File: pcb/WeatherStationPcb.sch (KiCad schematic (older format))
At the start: 7 parts, among them J1 Screw_Terminal_01x02, J2 Conn_01x06, J3 Conn_01x04, U1 MCP1755S-3302xCB, U3 ESP-01

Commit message: feat(pcb): update pcb
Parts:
- C1: value 100nF -> 10nF
- C2: value 10uF -> 10nF
- J2: value Conn_01x06 -> BME280
- J3: value Conn_01x04 -> BMP280
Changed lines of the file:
@@
 P 5400 2800
 F 0 "J3" V 5272 2980 50  0000 L CNN
-F 1 "Conn_01x04" V 5363 2980 50  0000 L CNN
+F 1 "BMP280" V 5363 2980 50  0000 L CNN
 F 2 "Connector_PinSocket_2.54mm:PinSocket_1x04_P2.54mm_Vertical" H 5400 2800 50  0001 C CNN
 F 3 "~" H 5400 2800 50  0001 C CNN
@@
 P 4150 2800
 F 0 "J2" V 4022 3080 50  0000 L CNN
-F 1 "Conn_01x06" V 4113 3080 50  0000 L CNN
+F 1 "BME280" V 4113 3080 50  0000 L CNN
 F 2 "Connector_PinSocket_2.54mm:PinSocket_1x06_P2.54mm_Vertical" H 4150 2800 50  0001 C CNN
 F 3 "~" H 4150 2800 50  0001 C CNN
@@
 P 3250 2550
 F 0 "C2" H 3365 2596 50  0000 L CNN
-F 1 "10uF" H 3365 2505 50  0000 L CNN
+F 1 "10nF" H 3365 2505 50  0000 L CNN
 F 2 "Capacitor_SMD:C_0805_2012Metric_Pad1.15x1.40mm_HandSolder" H 3288 2400 50  0001 C CNN
 F 3 "~" H 3250 2550 50  0001 C CNN
@@
 P 2100 2550
 F 0 "C1" H 2215 2596 50  0000 L CNN
-F 1 "100nF" H 2215 2505 50  0000 L CNN
+F 1 "10nF" H 2215 2505 50  0000 L CNN
 F 2 "Capacitor_SMD:C_0805_2012Metric_Pad1.15x1.40mm_HandSolder" H 2138 2400 50  0001 C CNN
 F 3 "~" H 2100 2550 50  0001 C CNN

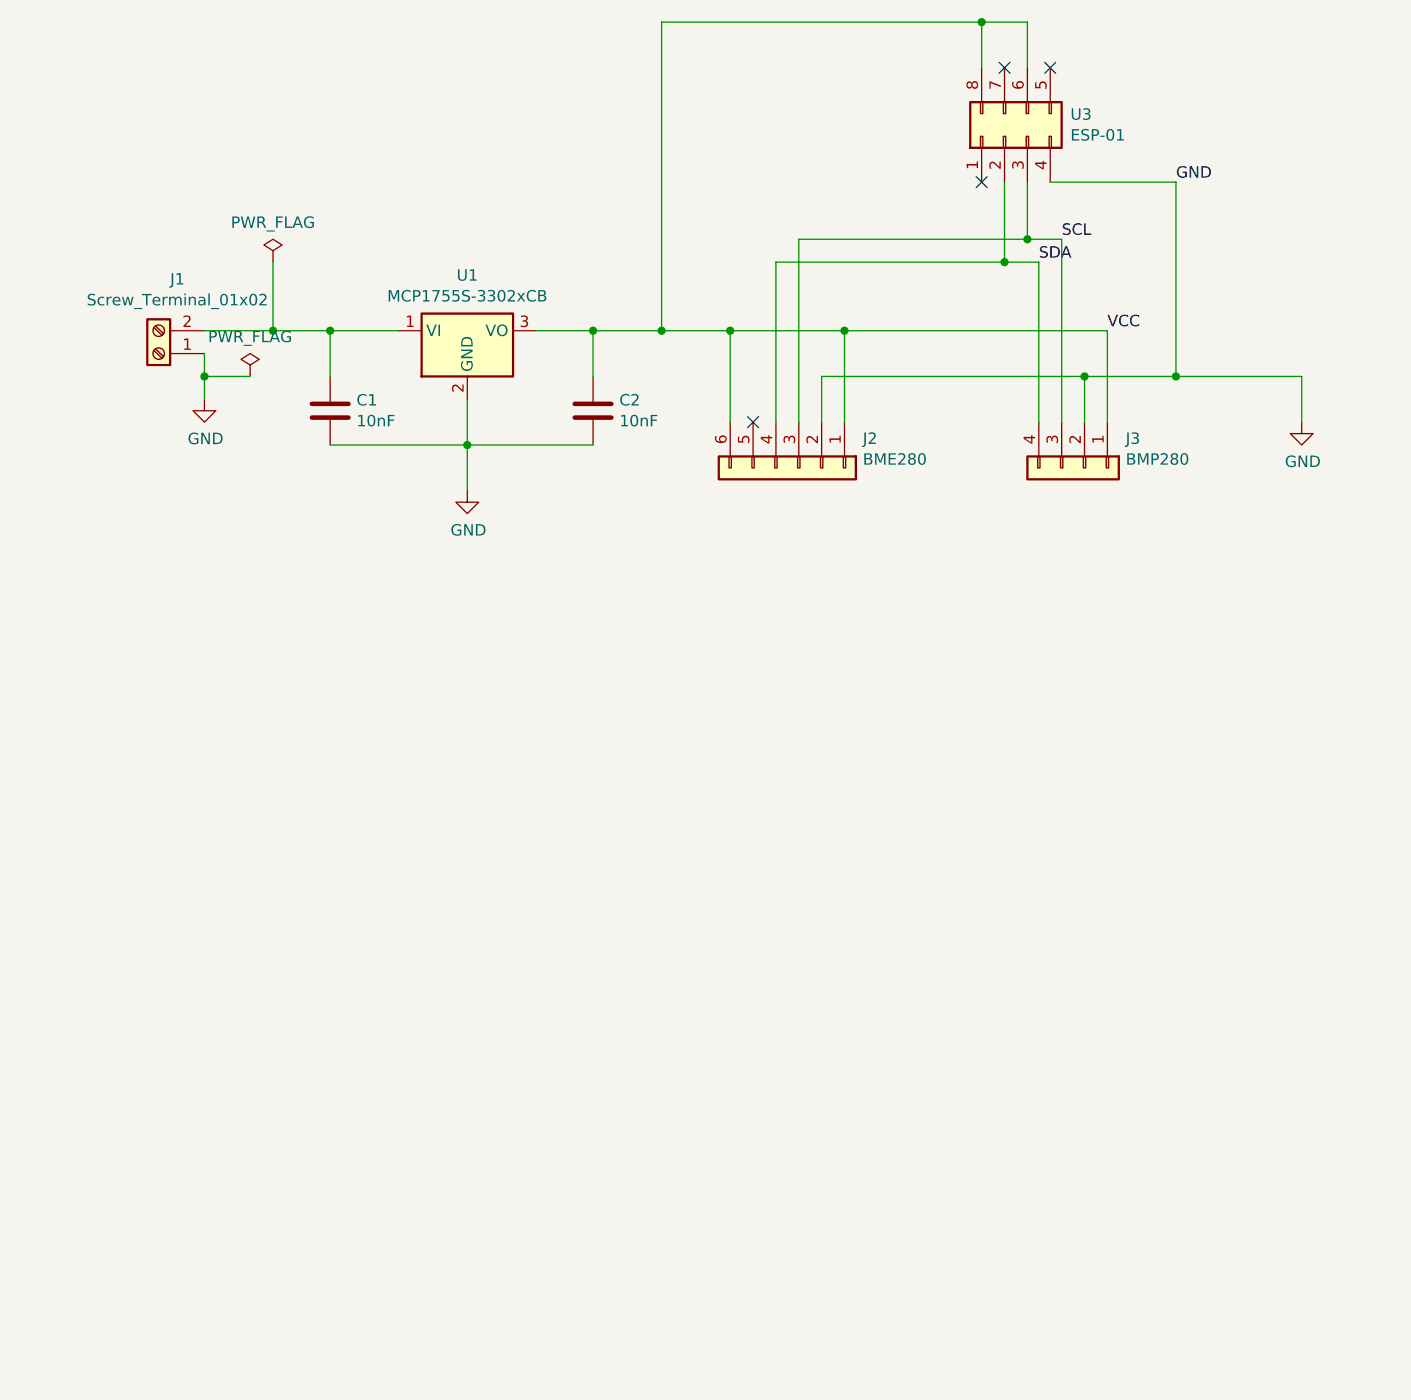
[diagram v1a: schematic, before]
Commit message: feat(pcb): update the pcb by adding voltage sensor
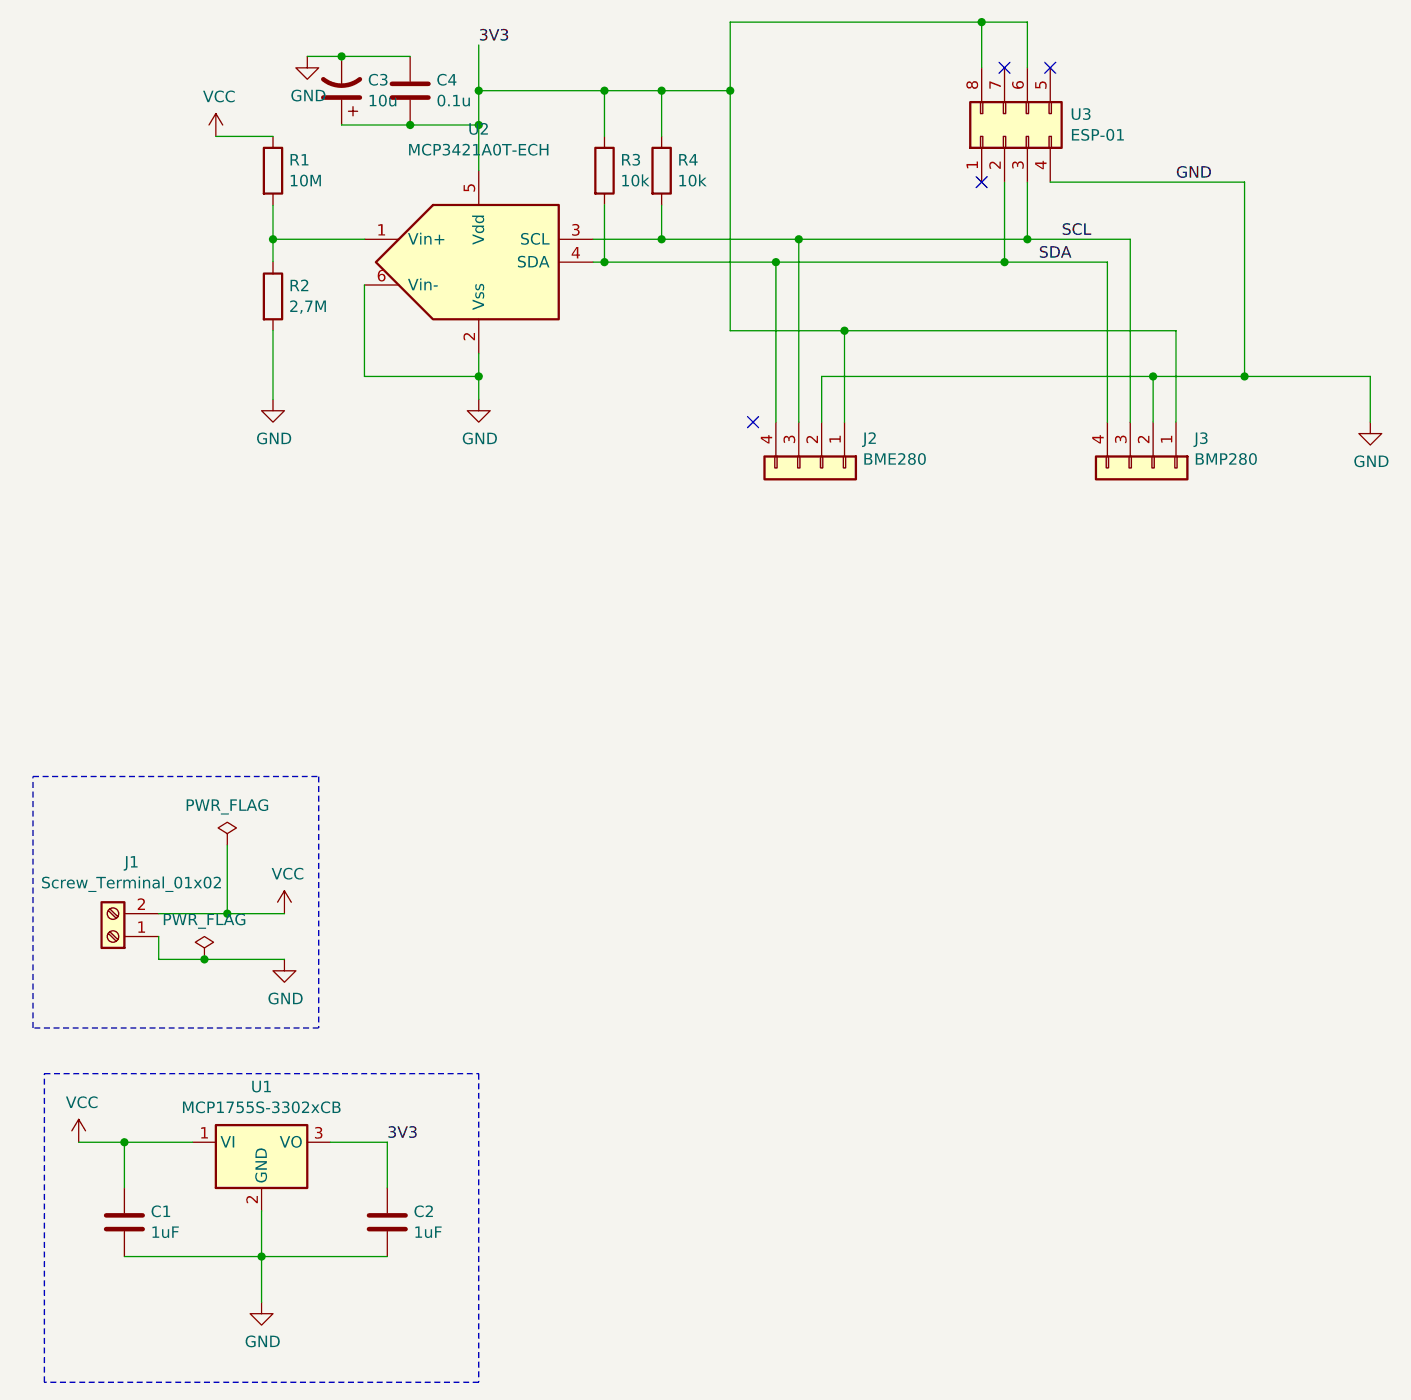
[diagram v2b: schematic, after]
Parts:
- removed J2: BME280, Connector_PinSocket_2.54mm:PinSocket_1x06_P2.54mm_Vertical, symbol Connector_Generic:Conn_01x06
- added C3: 10u, Capacitor_Tantalum_SMD:CP_EIA-6032-28_Kemet-C_Pad2.25x2.35mm_HandSolder, symbol Device:CP1
- added C4: 0.1u, Capacitor_SMD:C_0805_2012Metric_Pad1.15x1.40mm_HandSolder, symbol Device:C
- added J2: BME280, Connector_PinSocket_2.54mm:PinSocket_1x04_P2.54mm_Vertical, symbol Connector_Generic:Conn_01x04
- added R1: 10M, Resistor_SMD:R_0805_2012Metric_Pad1.15x1.40mm_HandSolder, symbol Device:R
- added R2: 2,7M, Resistor_SMD:R_0805_2012Metric_Pad1.15x1.40mm_HandSolder, symbol Device:R
- added R3, R4: 10k, Resistor_SMD:R_0805_2012Metric_Pad1.15x1.40mm_HandSolder, symbol Device:R
- added U2: MCP3421A0T-ECH, Package_TO_SOT_SMD:SOT-23-6_Handsoldering, symbol Analog_ADC:MCP3421A0T-ECH
- C1, C2: value 10nF -> 1uF
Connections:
- net GND: now also C3.2, C4.2, J2.2 (Pin_2), R2.2, U2.2 (Vss), U2.6 (Vin-)
- net SCL: now also J2.3 (Pin_3), R4.2, U2.3 (SCL)
- net SDA: now also J2.4 (Pin_4), R3.2, U2.4 (SDA)
- net VCC: now also C1.1, J1.2 (Pin_2), U1.1 (VI), R1.1; no longer C2.1, J3.1 (Pin_1), U1.3 (VO), U3.6 (CH_PD), U3.8 (VCC)
- new net: R1.2, R2.1, U2.1 (Vin+)
- new net 3V3: C2.1, C3.1, C4.1, J2.1 (Pin_1), J3.1 (Pin_1), R3.1, R4.1, U1.3 (VO), U2.5 (Vdd), U3.6 (CH_PD), U3.8 (VCC)
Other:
- moved on the sheet: C1, C2, J1, J3, U1
